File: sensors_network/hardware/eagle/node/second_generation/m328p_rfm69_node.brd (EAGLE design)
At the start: 50.8 x 41.9 mm, 37 parts, among them IC2 L6920, SW2 Node ID, U1 ATMEGA328P, U2 RFM69W, Y1 8MHz

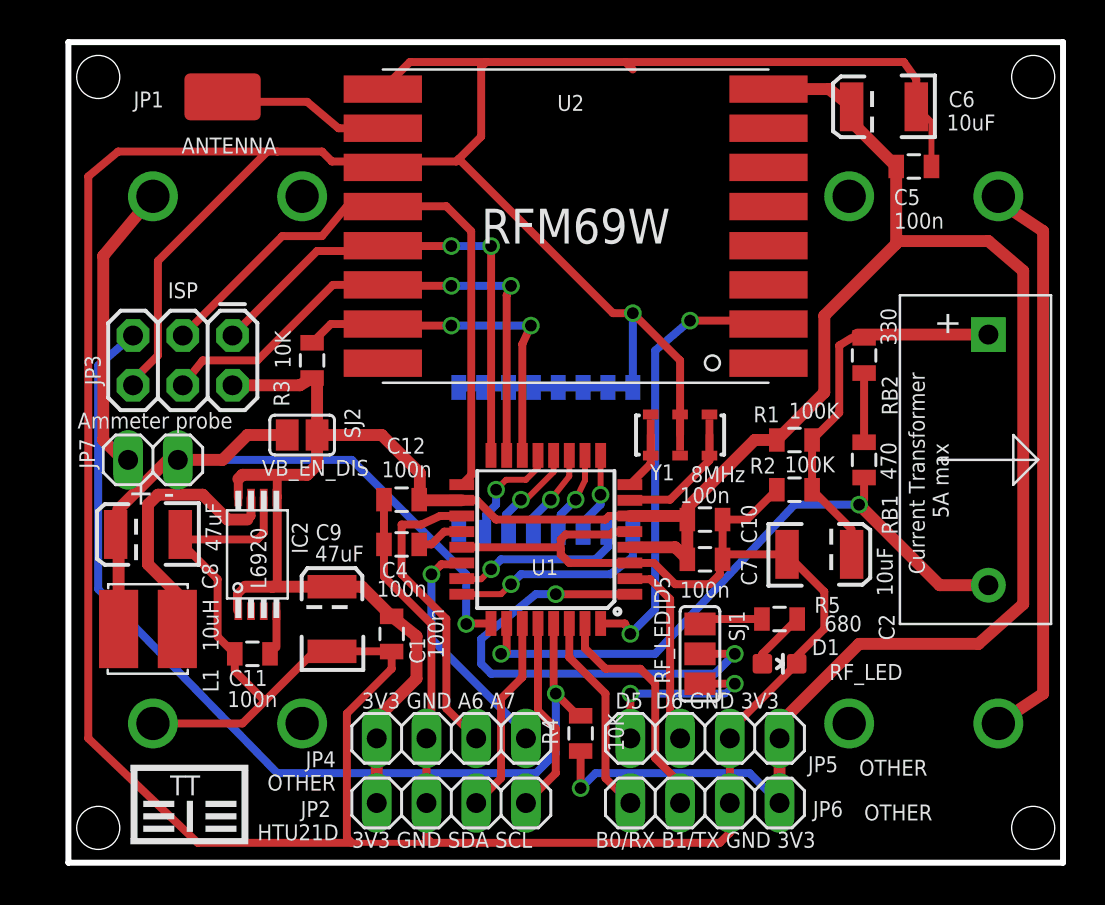
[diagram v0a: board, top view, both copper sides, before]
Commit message: [sensors_network] aaa battery powered node pcb final touches
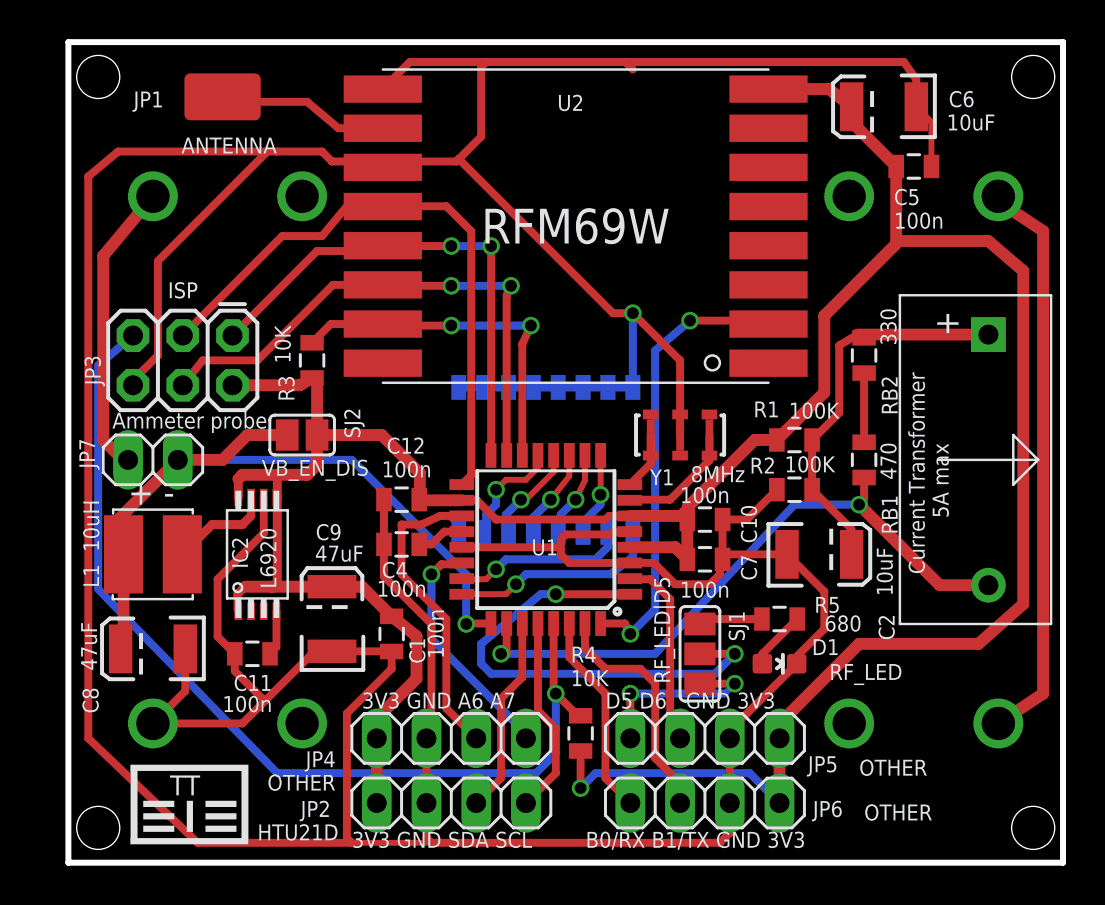
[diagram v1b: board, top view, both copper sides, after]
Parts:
- moved C8 5.85 mm to (4.06, 10.9)
- moved L1 3.82 mm to (4.06, 15.7)
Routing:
- net N$1: track 14.0 -> 5.26 mm
- net BATT_LVL: track 37.4 -> 38.2 mm
